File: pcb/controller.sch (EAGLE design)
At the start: 18 parts, among them IC1 74LS595D, IC2 74LS595D, U1 FT232RLSSOP, U2 ATMEGA328P, U3 ATMEGA328P_PDIP, X2 USB-SMD-NS

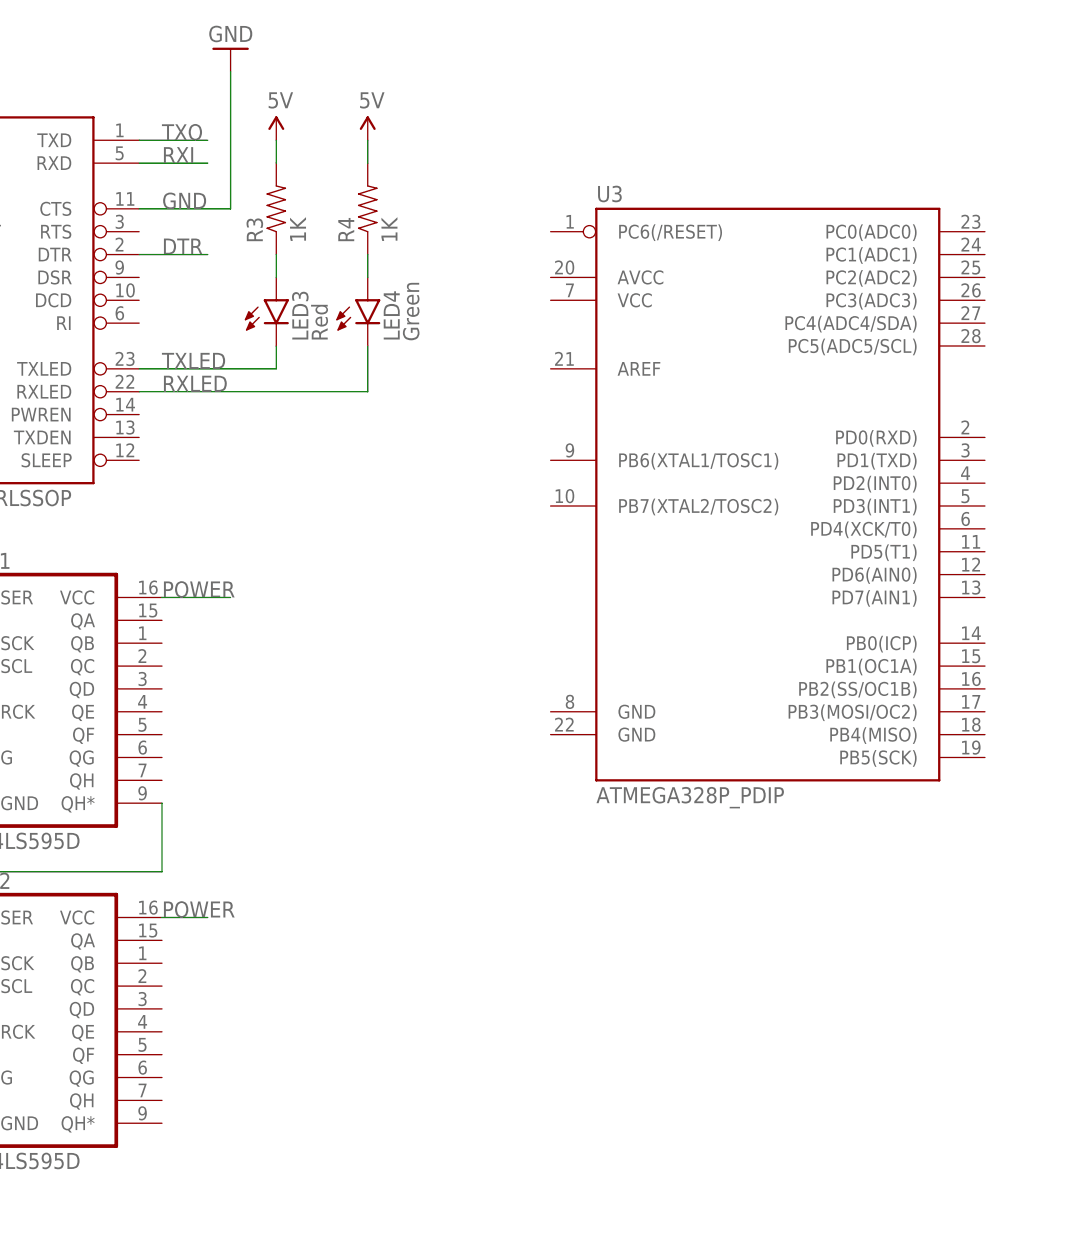
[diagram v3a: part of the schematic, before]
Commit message: Connected 5 RGB LED's
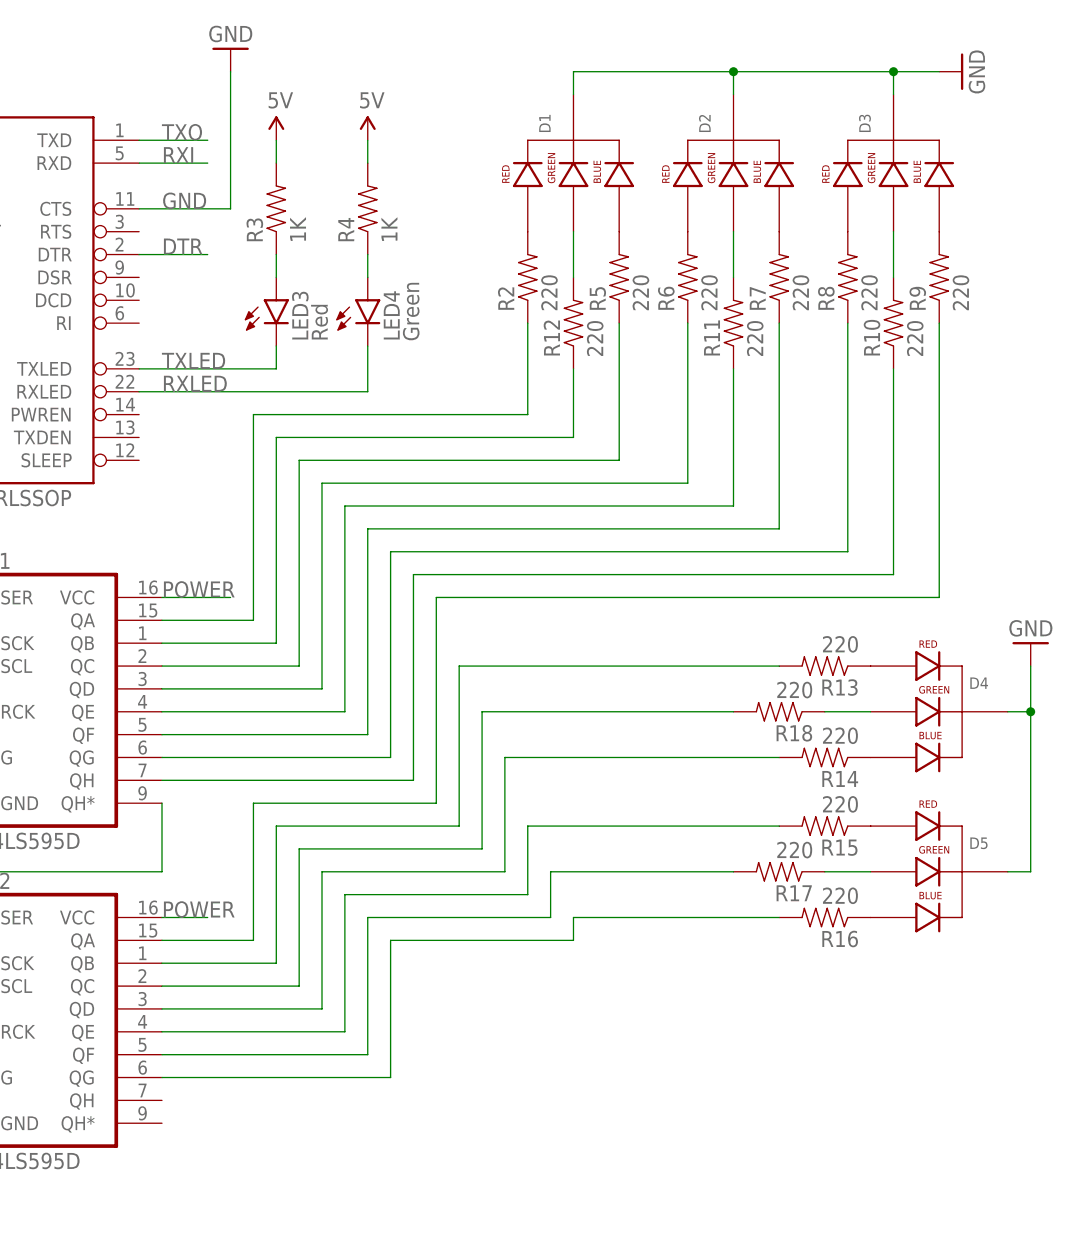
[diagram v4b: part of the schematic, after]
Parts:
- removed U3: ATMEGA328P_PDIP, SparkFun-DigitalIC:ATMEGA328P_PDIP
- added D1, D2, D3, D4, D5: LED-RGB-CC-THRUDIFFUSE, SparkFun-LED:LED-RGB-CC-THRUDIFFUSE
- added R10, R11, R12, R13, R14, R15, R16, R17, R18, R2, R5, R6, R7, R8, R9: 220, SparkFun-Resistors:RESISTOR0805-RES
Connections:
- new net N$10: D1.BLUE_CATHODE, R5.2
- new net N$11: D2.RED_CATHODE, R6.2
- new net N$12: D2.BLUE_CATHODE, R7.2
- new net N$13: D3.RED_CATHODE, R8.2
- new net N$14: D3.BLUE_CATHODE, R9.2
- new net N$15: D1.GREEN_CATHODE, R12.2
- new net N$16: D2.GREEN_CATHODE, R11.2
- new net N$17: D3.GREEN_CATHODE, R10.2
- new net N$18: IC1.QE, R11.1
- new net N$19: IC1.QF, R7.1
- new net N$20: IC1.QG, R8.1
- new net N$21: IC1.QH, R10.1
- new net N$22: IC2.QA, R9.1
- new net N$23: D5.RED_CATHODE, R15.1
- new net N$24: IC1.QA, R2.1
- new net N$25: IC1.QB, R12.1
- new net N$26: IC1.QC, R5.1
- new net N$27: IC1.QD, R6.1
- new net N$28: D5.BLUE_CATHODE, R16.1
- new net N$29: D4.RED_CATHODE, R13.1
- new net N$30: D4.BLUE_CATHODE, R14.1
- new net N$31: D4.GREEN_CATHODE, R18.1
- new net N$32: D5.GREEN_CATHODE, R17.1
- new net N$33: IC2.QB, R13.2
- new net N$34: IC2.QC, R18.2
- new net N$35: IC2.QD, R14.2
- new net N$36: IC2.QE, R15.2
- new net N$37: IC2.QF, R17.2
- new net N$38: IC2.QG, R16.2
- new net N$9: D1.RED_CATHODE, R2.2
- net GND: now also D1.CATHODE, D2.CATHODE, D3.CATHODE, D4.CATHODE, D5.CATHODE

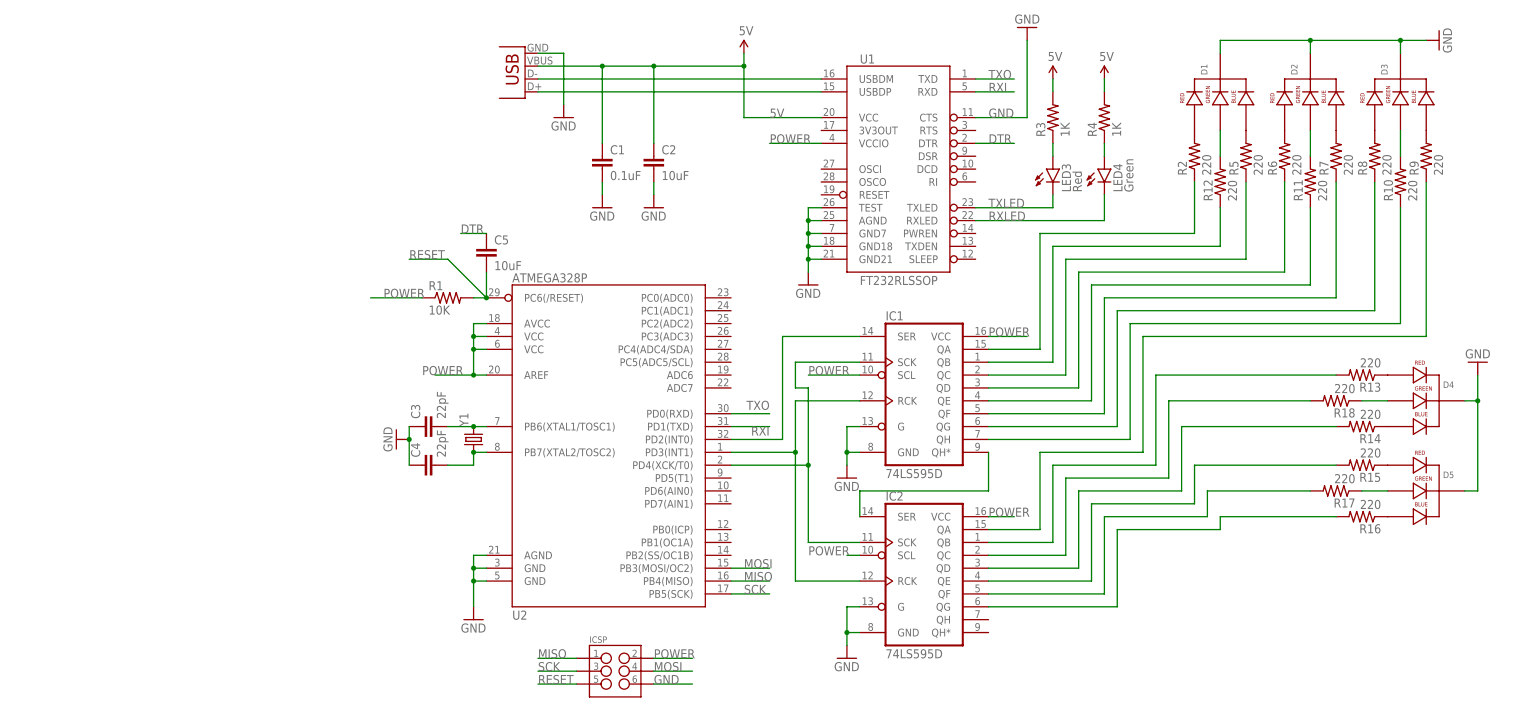
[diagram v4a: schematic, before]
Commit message: Re-connected RGB LEDs in a cleaner way
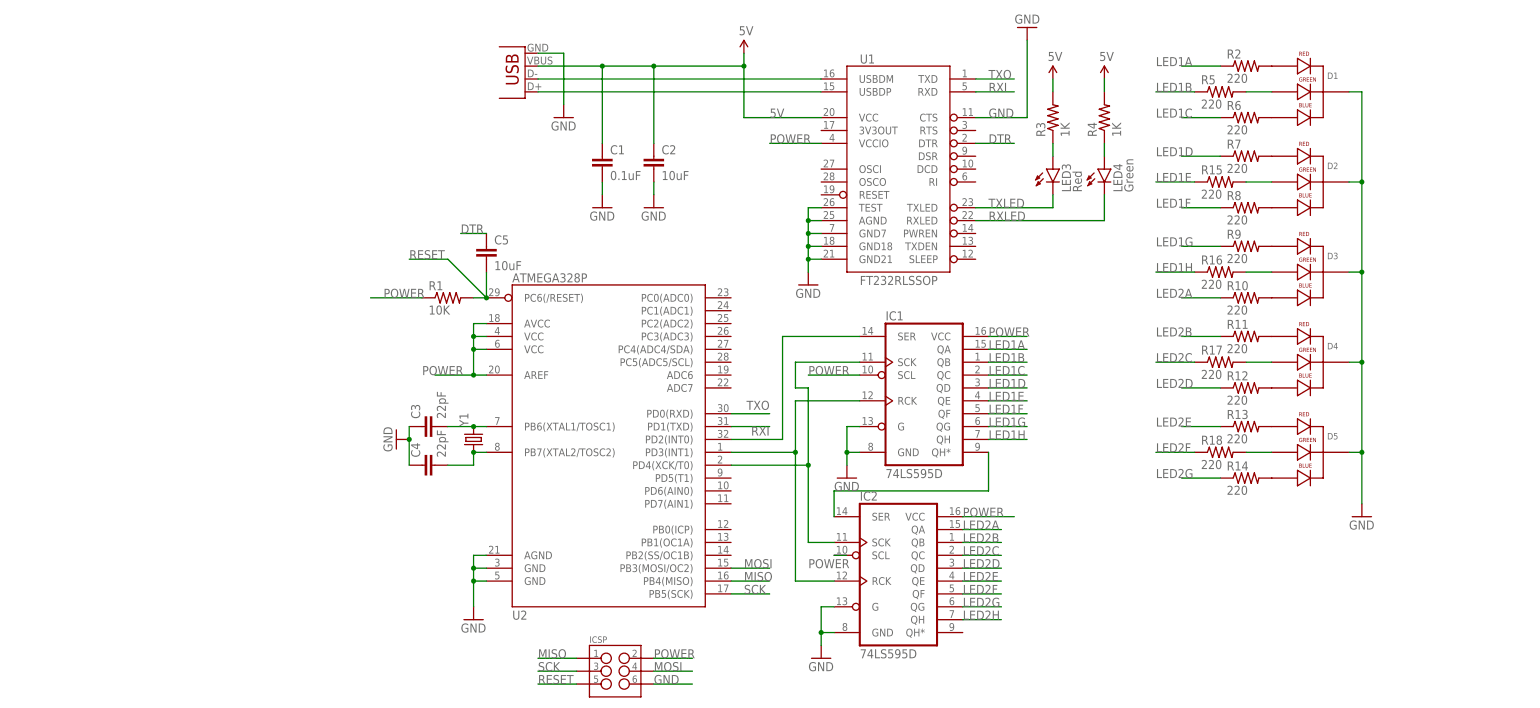
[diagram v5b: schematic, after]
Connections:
- net N$24 renamed LED1A
- removed net N$25: IC1.QB, R12.1
- removed net N$26: IC1.QC, R5.1
- removed net N$27: IC1.QD, R6.1
- removed net N$28: D5.BLUE_CATHODE, R16.1
- removed net N$29: D4.RED_CATHODE, R13.1
- removed net N$30: D4.BLUE_CATHODE, R14.1
- removed net N$31: D4.GREEN_CATHODE, R18.1
- removed net N$32: D5.GREEN_CATHODE, R17.1
- removed net N$33: IC2.QB, R13.2
- removed net N$34: IC2.QC, R18.2
- removed net N$35: IC2.QD, R14.2
- removed net N$36: IC2.QE, R15.2
- removed net N$37: IC2.QF, R17.2
- removed net N$38: IC2.QG, R16.2
- new net LED1B: IC1.QB, R5.1
- new net LED1C: IC1.QC, R6.1
- new net LED1D: IC1.QD, R7.1
- new net LED1E: IC1.QE, R15.1
- new net LED1F: IC1.QF, R8.1
- new net LED1G: IC1.QG, R9.1
- new net LED1H: IC1.QH, R16.1
- new net LED2A: IC2.QA, R10.1
- new net LED2B: IC2.QB, R11.1
- new net LED2C: IC2.QC, R17.1
- new net LED2D: IC2.QD, R12.1
- new net LED2E: IC2.QE, R13.1
- new net LED2F: IC2.QF, R18.1
- new net LED2G: IC2.QG, R14.1
- new net LED2H: IC2.QH
- net N$10: now also R6.2; no longer R5.2
- net N$11: now also R7.2; no longer R6.2
- net N$12: now also R8.2; no longer R7.2
- net N$13: now also R9.2; no longer R8.2
- net N$14: now also R10.2; no longer R9.2
- net N$15: now also D4.RED_CATHODE, R11.2; no longer D1.GREEN_CATHODE, R12.2
- net N$16: now also D4.BLUE_CATHODE, R12.2; no longer D2.GREEN_CATHODE, R11.2
- net N$17: now also D5.RED_CATHODE, R13.2; no longer D3.GREEN_CATHODE, R10.2
- net N$18: now also D5.BLUE_CATHODE, R14.2; no longer IC1.QE, R11.1
- net N$19: now also D1.GREEN_CATHODE, R5.2; no longer IC1.QF, R7.1
- net N$20: now also D2.GREEN_CATHODE, R15.2; no longer IC1.QG, R8.1
- net N$21: now also D3.GREEN_CATHODE, R16.2; no longer IC1.QH, R10.1
- net N$22: now also D4.GREEN_CATHODE, R17.2; no longer IC2.QA, R9.1
- net N$23: now also D5.GREEN_CATHODE, R18.2; no longer D5.RED_CATHODE, R15.1
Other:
- moved on the sheet: D1, D2, D3, D4, D5, IC2, R10, R11, R12, R13, R14, R15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

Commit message: Just before auto route
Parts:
- R10, R11, R12, R13, R14, R15, R16, R17, R18, R5, R6, R7, R8, R9: value 220 -> (none)
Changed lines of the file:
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@@
 <part name="GND10" library="SparkFun" deviceset="GND" device=""/>
 <part name="R2" library="SparkFun-Resistors" deviceset="RESISTOR" device="0805-RES" value="220"/>
-<part name="R5" library="SparkFun-Resistors" deviceset="RESISTOR" device="0805-RES" value="220"/>
-<part name="R6" library="SparkFun-Resistors" deviceset="RESISTOR" device="0805-RES" value="220"/>
-<part name="R7" library="SparkFun-Resistors" deviceset="RESISTOR" device="0805-RES" value="220"/>
-<part name="R8" library="SparkFun-Resistors" deviceset="RESISTOR" device="0805-RES" value="220"/>
-<part name="R9" library="SparkFun-Resistors" deviceset="RESISTOR" device="0805-RES" value="220"/>
-<part name="R10" library="SparkFun-Resistors" deviceset="RESISTOR" device="0805-RES" value="220"/>
-<part name="R11" library="SparkFun-Resistors" deviceset="RESISTOR" device="0805-RES" value="220"/>
-<part name="R12" library="SparkFun-Resistors" deviceset="RESISTOR" device="0805-RES" value="220"/>
-<part name="R13" library="SparkFun-Resistors" deviceset="RESISTOR" device="0805-RES" value="220"/>
-<part name="R14" library="SparkFun-Resistors" deviceset="RESISTOR" device="0805-RES" value="220"/>
-<part name="R15" library="SparkFun-Resistors" deviceset="RESISTOR" device="0805-RES" value="220"/>
-<part name="R16" library="SparkFun-Resistors" deviceset="RESISTOR" device="0805-RES" value="220"/>
-<part name="R17" library="SparkFun-Resistors" deviceset="RESISTOR" device="0805-RES" value="220"/>
-<part name="R18" library="SparkFun-Resistors" deviceset="RESISTOR" device="0805-RES" value="220"/>
+<part name="R5" library="SparkFun-Resistors" deviceset="RESISTOR" device="0805-RES"/>
+<part name="R6" library="SparkFun-Resistors" deviceset="RESISTOR" device="0805-RES"/>
+<part name="R7" library="SparkFun-Resistors" deviceset="RESISTOR" device="0805-RES"/>
+<part name="R8" library="SparkFun-Resistors" deviceset="RESISTOR" device="0805-RES"/>
+<part name="R9" library="SparkFun-Resistors" deviceset="RESISTOR" device="0805-RES"/>
+<part name="R10" library="SparkFun-Resistors" deviceset="RESISTOR" device="0805-RES"/>
+<part name="R11" library="SparkFun-Resistors" deviceset="RESISTOR" device="0805-RES"/>
+<part name="R12" library="SparkFun-Resistors" deviceset="RESISTOR" device="0805-RES"/>
+<part name="R13" library="SparkFun-Resistors" deviceset="RESISTOR" device="0805-RES"/>
+<part name="R14" library="SparkFun-Resistors" deviceset="RESISTOR" device="0805-RES"/>
+<part name="R15" library="SparkFun-Resistors" deviceset="RESISTOR" device="0805-RES"/>
+<part name="R16" library="SparkFun-Resistors" deviceset="RESISTOR" device="0805-RES"/>
+<part name="R17" library="SparkFun-Resistors" deviceset="RESISTOR" device="0805-RES"/>
+<part name="R18" library="SparkFun-Resistors" deviceset="RESISTOR" device="0805-RES"/>
 </parts>
 <sheets>
